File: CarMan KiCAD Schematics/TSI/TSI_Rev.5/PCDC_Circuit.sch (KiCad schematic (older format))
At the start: 55 parts, among them IC4 TS431ILT, J29 J29, K1 APAN3105, Q1 ZVP1320F, Q5 SI1302DL-T1-E3, U10 MC7805BDTRKG, U12 REF3033, U19 74HC00, U21 MCP6004, U29 SN74LVC1G08DCKR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

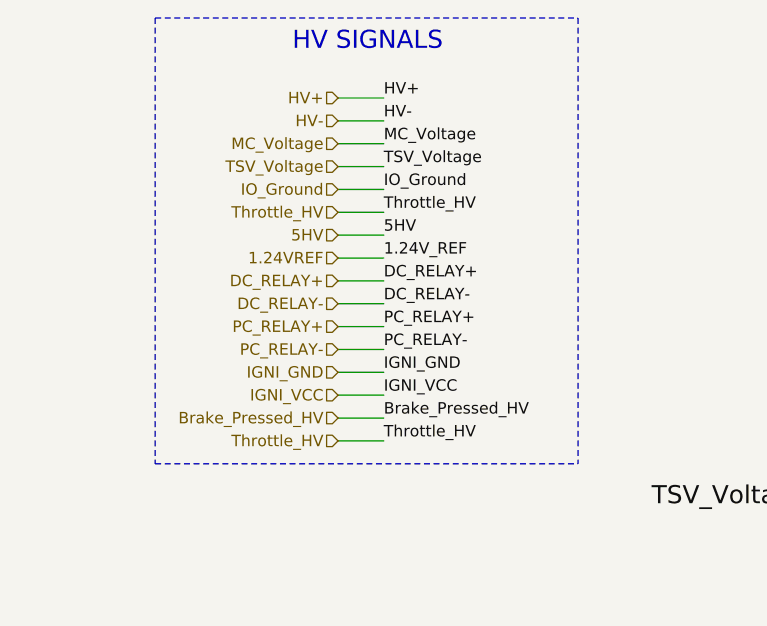
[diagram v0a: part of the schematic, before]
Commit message: TSI Signal Review ISSUES: - PCDC 'Pre_Charge_Ready' and 'PC_Ready' discrepancy - TSI Rev.4 IC1, IC4 -> PCDC & Isolators
REMOVED SIGNALS:
Throttle Plausibility
 - PC_Ready
 - Drive_BTN
 PCDC
 - HV+
 - HV-
 - Throttle_HV
 - IGNI_GND

STATUS LIGHTS & COCKPIT
- BP
- BP_RTN
- IMD_Status
- 5V
- Fault_LED
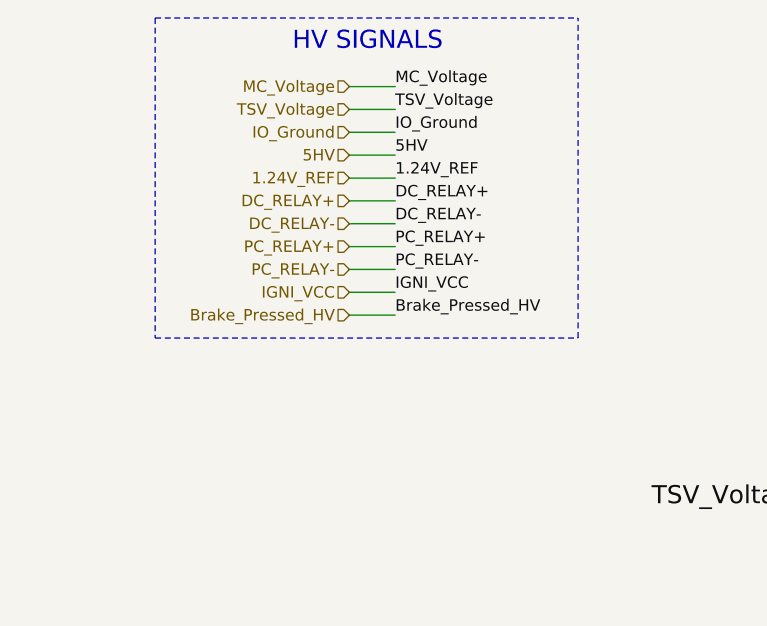
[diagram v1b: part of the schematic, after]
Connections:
- net 1.24VREF renamed 1.24V_REF
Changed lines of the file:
@@
 	1    0    0    -1
 $EndComp
-Text Label 1500 1050 0    50   ~ 0
+Text Label 1550 800  0    50   ~ 0
 MC_Voltage
-Text Label 1500 850  0    50   ~ 0
-HV+
-Wire Wire Line
-	1300 850  1500 850
-Wire Wire Line
-	1500 1050 1300 1050
-Text Label 1500 1350 0    50   ~ 0
-Throttle_HV
-Text Label 1500 1250 0    50   ~ 0
-IO_Ground
-Wire Wire Line
-	1500 1250 1300 1250
-Wire Wire Line
-	1500 1350 1300 1350
-Text Label 1500 950  0    50   ~ 0
-HV-
-Wire Wire Line
-	1500 950  1300 950
-Text Label 1500 1150 0    50   ~ 0
+Wire Wire Line
+	1550 800  1350 800
+Text Label 1550 1000 0    50   ~ 0
+IO_Ground
+Wire Wire Line
+	1550 1000 1350 1000
+Text Label 1550 900  0    50   ~ 0
 TSV_Voltage
 Wire Wire Line
-	1500 1150 1300 1150
+	1550 900  1350 900
 Text Notes 1100 650  0    79   ~ 0
 HV SIGNALS\n
-Text HLabel 1300 1350 0    50   Input ~ 0
-Throttle_HV
-Text HLabel 1300 1050 0    50   Input ~ 0
+Text HLabel 1350 800  0    50   Input ~ 0
 MC_Voltage
-Text HLabel 1300 950  0    50   Input ~ 0
-HV-
-Text HLabel 1300 850  0    50   Input ~ 0
-HV+
 $Comp
 L Device:R R56
@@
 Text Notes 4600 2250 0    47   ~ 0
 95% of Voltage
-Text HLabel 1300 1150 0    50   Input ~ 0
+Text HLabel 1350 900  0    50   Input ~ 0
 TSV_Voltage
-Text HLabel 1300 1250 0    50   Input ~ 0
-IO_Ground
-Text Label 1500 1550 0    50   ~ 0
+Text HLabel 1350 1000 0    50   Input ~ 0
+IO_Ground
+Text Label 1550 1200 0    50   ~ 0
 1.24V_REF
-Text Label 1500 1450 0    50   ~ 0
+Text Label 1550 1100 0    50   ~ 0
 5HV
 Wire Wire Line
-	1500 1450 1300 1450
-Wire Wire Line
-	1500 1550 1300 1550
-Text HLabel 1300 1550 0    50   Input ~ 0
-1.24VREF
-Text HLabel 1300 1450 0    50   Input ~ 0
+	1550 1100 1350 1100
+Wire Wire Line
+	1550 1200 1350 1200
+Text HLabel 1350 1200 0    50   Input ~ 0
+1.24V_REF
+Text HLabel 1350 1100 0    50   Input ~ 0
 5HV
 Text Label 1450 6850 0    50   ~ 0
@@
 Wire Notes Line
 	5700 5700 5700 11200
-Text Label 1500 1750 0    50   ~ 0
+Text Label 1550 1400 0    50   ~ 0
 DC_RELAY-
-Text Label 1500 1650 0    50   ~ 0
+Text Label 1550 1300 0    50   ~ 0
 DC_RELAY+
 Wire Wire Line
-	1500 1650 1300 1650
-Wire Wire Line
-	1500 1750 1300 1750
-Text HLabel 1300 1750 0    50   Input ~ 0
+	1550 1300 1350 1300
+Wire Wire Line
+	1550 1400 1350 1400
+Text HLabel 1350 1400 0    50   Input ~ 0
 DC_RELAY-
-Text HLabel 1300 1650 0    50   Input ~ 0
+Text HLabel 1350 1300 0    50   Input ~ 0
 DC_RELAY+
-Text Label 1500 1950 0    50   ~ 0
+Text Label 1550 1600 0    50   ~ 0
 PC_RELAY-
-Text Label 1500 1850 0    50   ~ 0
+Text Label 1550 1500 0    50   ~ 0
 PC_RELAY+
 Wire Wire Line
-	1500 1850 1300 1850
-Wire Wire Line
-	1500 1950 1300 1950
-Text HLabel 1300 1950 0    50   Input ~ 0
+	1550 1500 1350 1500
+Wire Wire Line
+	1550 1600 1350 1600
+Text HLabel 1350 1600 0    50   Input ~ 0
 PC_RELAY-
-Text HLabel 1300 1850 0    50   Input ~ 0
+Text HLabel 1350 1500 0    50   Input ~ 0
 PC_RELAY+
-Text Label 1500 2150 0    50   ~ 0
+Text Label 1550 1700 0    50   ~ 0
 IGNI_VCC
-Text Label 1500 2050 0    50   ~ 0
-IGNI_GND
-Wire Wire Line
-	1500 2050 1300 2050
-Wire Wire Line
-	1500 2150 1300 2150
-Text HLabel 1300 2150 0    50   Input ~ 0
+Wire Wire Line
+	1550 1700 1350 1700
+Text HLabel 1350 1700 0    50   Input ~ 0
 IGNI_VCC
-Text HLabel 1300 2050 0    50   Input ~ 0
-IGNI_GND
-Text Label 1500 2350 0    50   ~ 0
-Throttle_HV
-Text Label 1500 2250 0    50   ~ 0
+Text Label 1550 1800 0    50   ~ 0
 Brake_Pressed_HV
 Wire Wire Line
-	1500 2250 1300 2250
-Wire Wire Line
-	1500 2350 1300 2350
-Text HLabel 1300 2350 0    50   Input ~ 0
-Throttle_HV
-Text HLabel 1300 2250 0    50   Input ~ 0
+	1550 1800 1350 1800
+Text HLabel 1350 1800 0    50   Input ~ 0
 Brake_Pressed_HV
 Wire Wire Line
@@
 Text Notes 2250 5650 0    197  ~ 0
 HIGH VOLTAGE\n
-Wire Notes Line
-	500  500  500  2450
-Wire Notes Line
-	500  2450 2350 2450
-Wire Notes Line
-	2350 500  2350 2450
 Wire Notes Line
 	500  500  2350 500
@@
 Text Notes 2900 10000 0    47   ~ 0
 Diagnostics Pin:\nEasy hookup to \nAIRS-/GLV RTN
+Wire Notes Line
+	500  1900 2350 1900
+Wire Notes Line
+	2350 1900 2350 500
+Wire Notes Line
+	500  500  500  1900
 $EndSCHEMATC

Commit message: TSI Updated
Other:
- note added: "3.3V Reference Voltage"
- note added: "VOLTAGE REFERENCES & REGULATORS\n(HIGH VOLTAGE)"
- note removed: "HV"
- note removed: "VOLTAGE REFERENCES & REGULATORS"
- moved on the sheet: C1, C12, IC4, R101, R46, RV5, U10, U12

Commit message: Contemplated homicide and fixed PC schematic
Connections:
- net at U21.13 (-), U21.14: now also U40.5 (+); no longer U40.6 (-)
- net at RV3.2: now also U40.6 (-); no longer U40.5 (+)
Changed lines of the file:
@@
 Text Label 5850 3500 0    55   ~ 0
 PC_Ready_HV
-Text Notes 5800 3500 2    55   ~ 0
-~R\n
 Text Notes 7600 3900 2    55   ~ 0
 ~R\n
@@
 Text Label 15250 3900 2    47   ~ 0
 IGNI_VCC
-Text Label 15250 4100 2    50   ~ 0
-Pre_Charge_Ready
 Wire Notes Line
 	13400 3750 14550 3750
@@
 F 3 "http://ww1.microchip.com/downloads/en/DeviceDoc/21733j.pdf" H 5400 3700 50  0001 C CNN
 	2    5350 3500
-	1    0    0    -1
+	1    0    0    1
 $EndComp
 Text Label 6600 2100 0    47   ~ 0
@@
 	12950 7250 14350 7250
 Wire Wire Line
-	14200 4100 15250 4100
-Wire Wire Line
 	14300 3050 15200 3050
 Wire Wire Line
@@
 Wire Wire Line
 	14200 3900 15250 3900
-Connection ~ 14200 3900
-Wire Wire Line
-	14200 3900 14200 4100
 Wire Wire Line
 	1350 1800 2150 1800

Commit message: - Updating TSI
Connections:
- net 3.3_VREF renamed 3.3HV_REF
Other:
- note added: "3.3HV Reference Voltage"
- note removed: "3.3V Reference Voltage"
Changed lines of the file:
@@
 	1    0    0    -1
 $EndComp
-Text Label 9900 4250 0    47   ~ 0
-3.3_VREF
-Wire Wire Line
-	9900 4250 10250 4250
+Text Label 9850 4250 0    47   ~ 0
+3.3HV_REF
 Wire Wire Line
 	10250 4050 9500 4050
@@
 5HV
 Text Label 13550 9050 2    59   ~ 0
-3.3_VREF
+3.3HV_REF
 Text Label 12100 9500 0    59   ~ 0
 IO_Ground
@@
 	500  500  500  1900
 Text Notes 11600 9800 0    79   ~ 0
-3.3V Reference Voltage
+3.3HV Reference Voltage
 Wire Wire Line
 	15600 8950 15350 8950
@@
 Wire Wire Line
 	2850 2650 3700 2650
+Wire Wire Line
+	9850 4250 10250 4250
 $EndSCHEMATC

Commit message: Edited Throttle Plausibility Braking circuit (was 24V, not AIRS+), renamed signals for clearer BRAKE_IN & BRAKE_OUT signals, BRAKE_OUT = Brake_Light
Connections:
- net Brake_Pressed renamed BRAKE_OUT
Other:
- note added: "If car brake is pressed,\niso conducts"
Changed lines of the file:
@@
 	5400 7150 5250 7150
 Text Label 4200 7150 0    59   ~ 0
-Brake_Pressed
+BRAKE_OUT
 Text Label 4200 7350 0    59   ~ 0
 GLV_RTN
@@
 Safety_Loop
 Text Label 1950 6750 2    50   ~ 0
-Brake_Pressed
+BRAKE_OUT
 Text Label 1950 6350 2    50   ~ 0
 3.3V
@@
 5V
 Text HLabel 1250 6750 0    50   Input ~ 0
-Brake_Pressed
+BRAKE_OUT
 Text Label 1950 6550 2    50   ~ 0
 GLV_RTN
@@
 Wire Wire Line
 	9850 4250 10250 4250
+Text Notes 4700 7550 0    51   ~ 0
+If car brake is pressed,\niso conducts
 $EndSCHEMATC

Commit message: Renumbered headers & changed some footprints
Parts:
- J30: renamed from J29; value J29 -> GLV Hook-up Pin; footprint Connector_PinHeader_1.00mm:PinHeader_1x01_P1.00mm_Vertical -> Connector_PinSocket_2.54mm:PinSocket_1x01_P2.54mm_Vertical
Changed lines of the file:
@@
 P 3600 9850
 AR Path="/5F98EBE9/60319B93" Ref="J?"  Part="1"
-AR Path="/6196BF15/60319B93" Ref="J29"  Part="1"
-F 0 "J29" V 3700 9800 50  0000 L CNN
-F 1 "J29" V 3700 9650 50  0001 L CNN
-F 2 "Connector_PinHeader_1.00mm:PinHeader_1x01_P1.00mm_Vertical" H 3600 9850 50  0001 C CNN
+AR Path="/6196BF15/60319B93" Ref="J30"  Part="1"
+F 0 "J30" V 3700 9800 50  0000 L CNN
+F 1 "GLV Hook-up Pin" V 3700 9650 50  0001 L CNN
+F 2 "Connector_PinSocket_2.54mm:PinSocket_1x01_P2.54mm_Vertical" H 3600 9850 50  0001 C CNN
 F 3 "~" H 3600 9850 50  0001 C CNN
 	1    3600 9850

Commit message: ADDED K1-APAN3105 Relay to symbol and footprint libraries
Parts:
- K1: footprint Relay_THT:Relay_SPST_Finder_32.21-x300 -> TSI_Rev_2021_Footprint_Lib:RELAY_APAN3105; symbol Relay:FINDER-36.11-4301 -> CarMan_KiCAD_Library:APAN3105
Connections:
- net 5HV: now also K1.C1; no longer K1.A1
- net IGNI_VCC: now also K1.NO; no longer K1.11
- net PC_RELAY+: now also K1.M; no longer K1.14
- net at D7.1 (K), D8.2 (A), JP4.2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: now also K1.C2; no longer K1.A2
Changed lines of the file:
@@
 Connection ~ 12400 3850
 $Comp
-L Relay:FINDER-36.11-4301 K1
+L CarMan_KiCAD_Library:APAN3105 K1
 U 1 1 5F9E72DA
-P 14000 3450
-F 0 "K1" H 14000 3900 50  0000 L CNN
-F 1 "APAN3105" H 13850 3800 50  0000 L CNN
-F 2 "Relay_THT:Relay_SPST_Finder_32.21-x300" H 15270 3420 50  0001 C CNN
-F 3 "http://gfinder.findernet.com/assets/Series/356/S36EN.pdf" H 14000 3450 50  0001 C CNN
-	1    14000 3450
+P 13900 3450
+F 0 "K1" H 13900 3900 50  0000 L CNN
+F 1 "APAN3105" H 13750 3800 50  0000 L CNN
+F 2 "TSI_Rev_2021_Footprint_Lib:RELAY_APAN3105" H 15170 3420 50  0001 C CNN
+F 3 "http://gfinder.findernet.com/assets/Series/356/S36EN.pdf" H 13900 3450 50  0001 C CNN
+	1    13900 3450
 	1    0    0    -1
 $EndComp
 Text Label 11850 4700 0    55   ~ 0
 IO_Ground
-Wire Wire Line
-	13050 3050 13800 3050
-Wire Wire Line
-	13800 3050 13800 3150
-Connection ~ 13050 3050
-Wire Wire Line
-	13800 3750 13800 3850
-Wire Wire Line
-	13800 3850 13050 3850
 Connection ~ 13050 3850
-Wire Wire Line
-	14300 3050 14300 3150
-Text Label 15200 3050 2    50   ~ 0
+Text Label 15350 3050 2    50   ~ 0
 24HV
-Text Label 15250 3900 2    47   ~ 0
+Text Label 15350 3850 2    47   ~ 0
 IGNI_VCC
 Wire Notes Line
@@
 	12950 7250 14350 7250
 Wire Wire Line
-	14300 3050 15200 3050
-Wire Wire Line
-	14200 3750 14200 3900
-Wire Wire Line
-	14200 3900 15250 3900
+	14300 3850 15350 3850
 Wire Wire Line
 	1350 1800 2150 1800
@@
 Text Notes 4700 7550 0    51   ~ 0
 If car brake is pressed,\niso conducts
+Wire Wire Line
+	13050 3050 13600 3050
+Wire Wire Line
+	13600 3050 13600 3250
+Connection ~ 13050 3050
+Wire Wire Line
+	13600 3550 13600 3850
+Wire Wire Line
+	13600 3850 13050 3850
+Wire Wire Line
+	14300 3550 14300 3850
+Wire Wire Line
+	14300 3050 14300 3350
+Wire Wire Line
+	14300 3050 15350 3050
 $EndSCHEMATC

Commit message: Updated parts U19 & U12 to have their actual names so we can order them in the future
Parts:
- U12: Mouser Part # (none) -> REF3033AIDBZT
- U19: value 74HC00 -> SN74HC00APWR
- U19: value 74HC00 -> SN74HC00APWR; Mouser Link (none) -> https://www.mouser.com/ProductDetail/Texas-Instruments/SN74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
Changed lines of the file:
@@
 P 7100 2950
 F 0 "U19" H 7100 2950 50  0000 C CNN
-F 1 "74HC00" H 7200 3150 50  0000 C CNN
+F 1 "SN74HC00APWR" H 7200 3150 50  0000 C CNN
 F 2 "TSI_Rev_2021_Footprint_Lib:SOIC127P600X175-14N" H 7100 2950 50  0001 C CNN
 F 3 "http://www.ti.com/lit/gpn/sn74hc00" H 7100 2950 50  0001 C CNN
+F 4 "https://www.mouser.com/ProductDetail/Texas-Instruments/SN74HC00APWR?qs=6ZVwTuetbD5Of4SwrWZoMw%3D%3D" H 7100 2950 50  0001 C CNN "Mouser Link"
 	1    7100 2950
 	1    0    0    -1
@@
 P 5400 4300
 F 0 "U19" H 5400 4300 50  0000 C CNN
-F 1 "74HC00" H 5400 4534 50  0000 C CNN
+F 1 "SN74HC00APWR" H 5400 4534 50  0000 C CNN
 F 2 "TSI_Rev_2021_Footprint_Lib:SOIC127P600X175-14N" H 5400 4300 50  0001 C CNN
 F 3 "http://www.ti.com/lit/gpn/sn74hc00" H 5400 4300 50  0001 C CNN
@@
 P 8050 3050
 F 0 "U19" H 8050 3050 50  0000 C CNN
-F 1 "74HC00" H 8050 3250 50  0000 C CNN
+F 1 "SN74HC00APWR" H 8050 3250 50  0000 C CNN
 F 2 "TSI_Rev_2021_Footprint_Lib:SOIC127P600X175-14N" H 8050 3050 50  0001 C CNN
 F 3 "http://www.ti.com/lit/gpn/sn74hc00" H 8050 3050 50  0001 C CNN
@@
 P 8050 3800
 F 0 "U19" H 8050 3800 50  0000 C CNN
-F 1 "74HC00" H 8050 3600 50  0000 C CNN
+F 1 "SN74HC00APWR" H 8050 3600 50  0000 C CNN
 F 2 "TSI_Rev_2021_Footprint_Lib:SOIC127P600X175-14N" H 8050 3800 50  0001 C CNN
 F 3 "http://www.ti.com/lit/gpn/sn74hc00" H 8050 3800 50  0001 C CNN
@@
 P 7500 2100
 F 0 "U19" V 7650 2100 50  0000 C CNN
-F 1 "74HC00" V 7250 2100 50  0000 C CNN
+F 1 "SN74HC00APWR" V 7250 2100 50  0000 C CNN
 F 2 "TSI_Rev_2021_Footprint_Lib:SOIC127P600X175-14N" H 7500 2100 50  0001 C CNN
 F 3 "http://www.ti.com/lit/gpn/sn74hc00" H 7500 2100 50  0001 C CNN
@@
 F 1 "REF3033" H 12521 9005 50  0000 R CIN
 F 2 "Package_TO_SOT_SMD:SOT-23" H 12750 8600 50  0001 C CIN
-F 3 "http://www.ti.com/lit/ds/symlink/ref3033.pdf" H 12850 8700 50  0001 C CIN
+F 3 "https://www.ti.com/lit/ds/symlink/ref3033.pdf" H 12850 8700 50  0001 C CIN
+F 4 "REF3033AIDBZT" H 12750 9050 50  0001 C CNN "Mouser Part #"
 	1    12750 9050
 	1    0    0    -1
